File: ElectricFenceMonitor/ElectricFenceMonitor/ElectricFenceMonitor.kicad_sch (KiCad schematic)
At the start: 32 parts, among them J1 Fence wire, J2 Fence ground, J3 Power, J4 Programming, Q1 BC548, U1 Ra01_Breakout_Module, U2 PICAXE-14M2

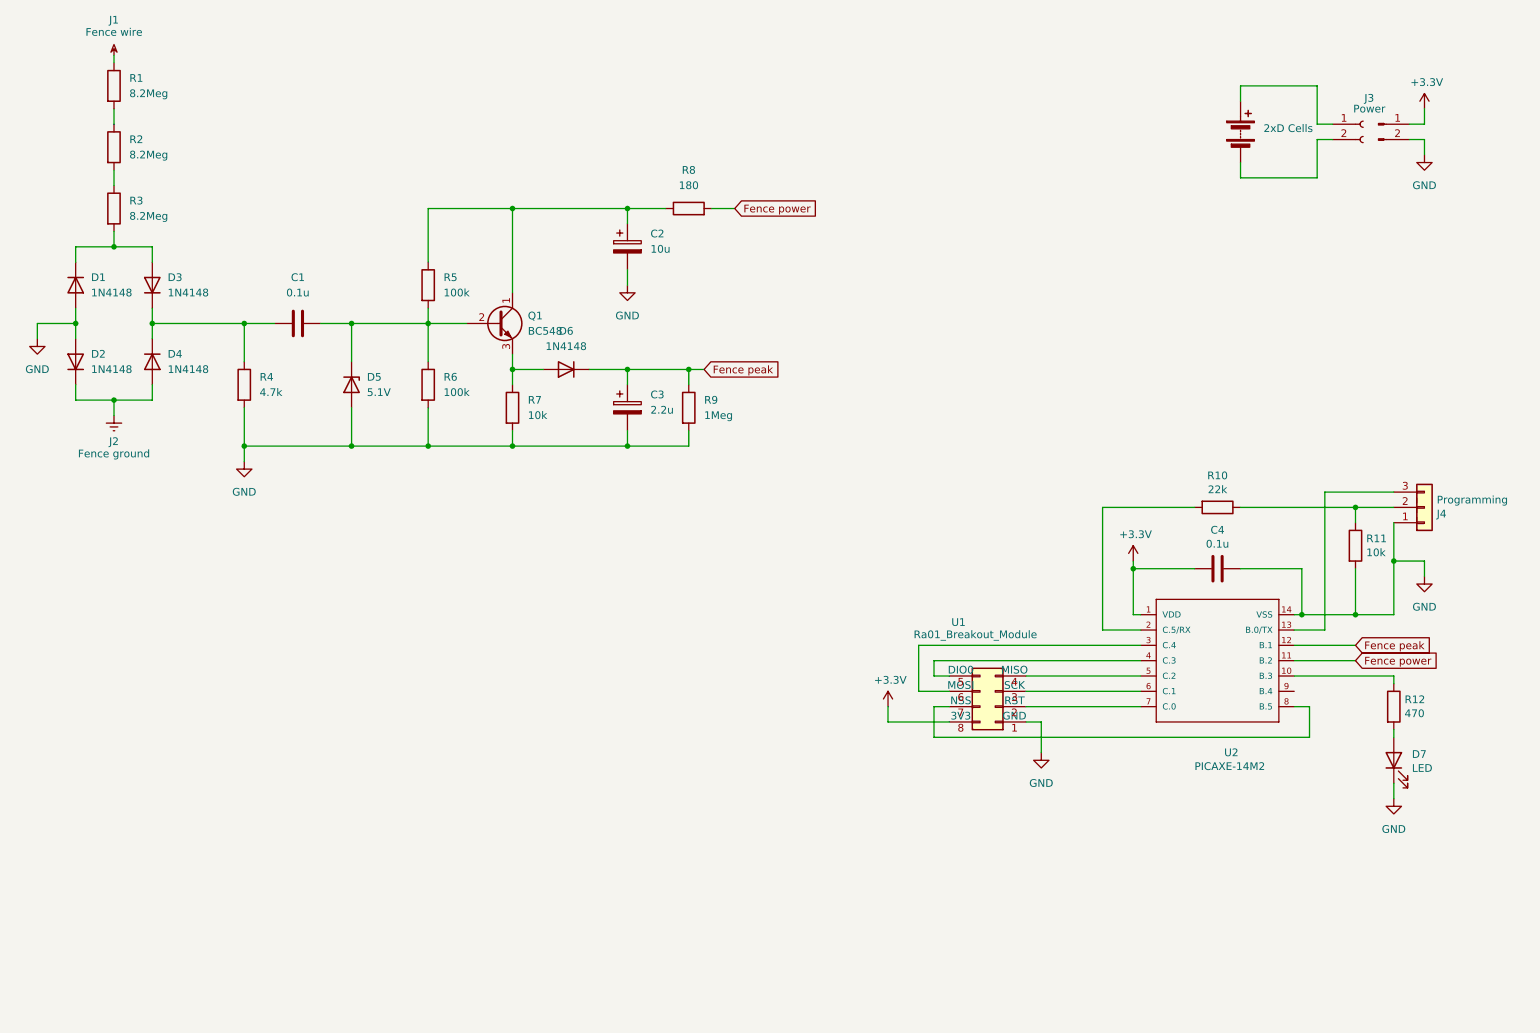
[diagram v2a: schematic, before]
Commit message: Electric fence monitor schematic updated, layout redone
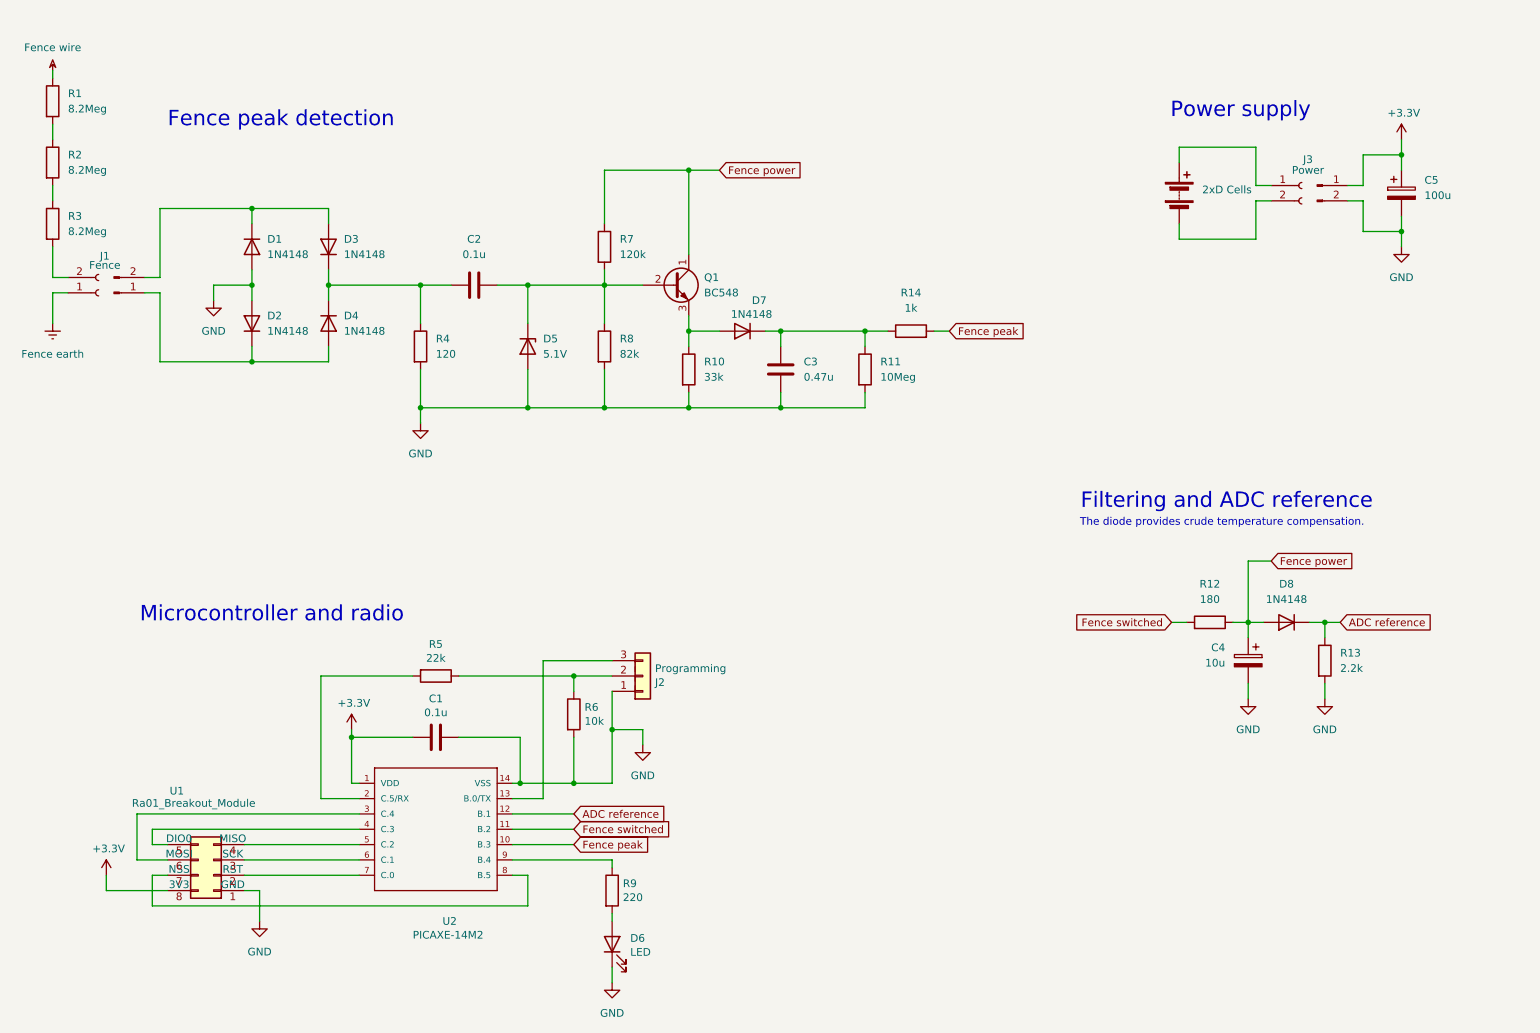
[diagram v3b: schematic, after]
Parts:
- removed C2: 10u, Capacitor_THT:CP_Radial_D6.3mm_P2.50mm, symbol Device:C_Polarized
- removed C3: 2.2u, Capacitor_THT:C_Axial_L5.1mm_D3.1mm_P10.00mm_Horizontal, symbol Device:C_Polarized
- removed J1: Fence wire, MountingHole:MountingHole_3.5mm_Pad_Via, symbol power:HT
- removed J2: Fence ground, MountingHole:MountingHole_3.5mm_Pad_Via, symbol power:GNDREF
- removed R8: 180, Resistor_THT:R_Axial_DIN0207_L6.3mm_D2.5mm_P15.24mm_Horizontal, symbol Device:R
- added #J1: Conn_01x02_Socket, symbol Connector:Conn_01x02_Socket
- added C3: 0.47u, Capacitor_THT:C_Disc_D5.0mm_W2.5mm_P5.00mm, symbol Device:C
- added C4: 10u, Capacitor_THT:CP_Radial_D13.0mm_P5.00mm, symbol Device:C_Polarized
- added C5: 100u, Capacitor_THT:CP_Radial_D13.0mm_P5.00mm, symbol Device:C_Polarized
- added D8: 1N4148, Diode_THT:D_DO-35_SOD27_P5.08mm_Vertical_KathodeUp, symbol Diode:1N4148
- added J1: Fence, TerminalBlock_Phoenix:TerminalBlock_Phoenix_MKDS-1,5-2-5.08_1x02_P5.08mm_Horizontal, symbol Connector:Conn_01x02_Pin
- added R12: 180, Resistor_THT:R_Axial_DIN0207_L6.3mm_D2.5mm_P7.62mm_Horizontal, symbol Device:R
- added R13: 2.2k, Resistor_THT:R_Axial_DIN0207_L6.3mm_D2.5mm_P7.62mm_Horizontal, symbol Device:R
- added R14: 1k, Resistor_THT:R_Axial_DIN0207_L6.3mm_D2.5mm_P7.62mm_Horizontal, symbol Device:R
- D2: footprint Diode_THT:D_DO-35_SOD27_P7.62mm_Horizontal -> Diode_THT:D_DO-35_SOD27_P5.08mm_Vertical_KathodeUp
- D4: footprint Diode_THT:D_DO-35_SOD27_P10.16mm_Horizontal -> Diode_THT:D_DO-35_SOD27_P7.62mm_Horizontal
- D5: footprint Diode_THT:D_A-405_P7.62mm_Horizontal -> Diode_THT:D_A-405_P10.16mm_Horizontal
- D7: renamed from D6; footprint Diode_THT:D_DO-35_SOD27_P5.08mm_Vertical_AnodeUp -> Diode_THT:D_DO-35_SOD27_P7.62mm_Horizontal
- R10: renamed from R7; value 10k -> 33k; footprint Resistor_THT:R_Axial_DIN0207_L6.3mm_D2.5mm_P7.62mm_Horizontal -> Resistor_THT:R_Axial_DIN0309_L9.0mm_D3.2mm_P12.70mm_Horizontal
- R11: renamed from R9; value 1Meg -> 10Meg; footprint Resistor_THT:R_Axial_DIN0207_L6.3mm_D2.5mm_P10.16mm_Horizontal -> Resistor_THT:R_Axial_DIN0207_L6.3mm_D2.5mm_P5.08mm_Vertical
- R4: value 4.7k -> 120
- R7: renamed from R5; value 100k -> 120k
- R8: renamed from R6; value 100k -> 82k; footprint Resistor_THT:R_Axial_DIN0207_L6.3mm_D2.5mm_P7.62mm_Horizontal -> Resistor_THT:R_Axial_DIN0207_L6.3mm_D2.5mm_P10.16mm_Horizontal
- R9: renamed from R12; value 470 -> 220; footprint Resistor_THT:R_Axial_DIN0309_L9.0mm_D3.2mm_P25.40mm_Horizontal -> Resistor_THT:R_Axial_DIN0207_L6.3mm_D2.5mm_P7.62mm_Horizontal
- renumbered #J1 to #J2, C4 to C1, C1 to C2, D7 to D6, J4 to J2, R10 to R5, R11 to R6
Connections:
- net +3.3V: now also C5.1
- net Fence peak: now also U2.10 (B.3), R14.2; no longer D7.1 (K), R11.1, U2.12 (B.1)
- net Fence power: now also Q1.1 (C), R7.1, C4.1, D8.2 (A), R12.1; no longer U2.11 (B.2)
- net GND: now also C3.1, C4.2, C5.2, R13.2
- net at D2.1 (K), D4.2 (A): now also J1.1 (Pin_1)
- net at D1.1 (K), D3.2 (A): now also J1.2 (Pin_2); no longer R3.2
- net Fence wire: now reaches R1.1
- net at R9.1: now also U2.9 (B.4); no longer U2.10 (B.3)
- new net: #J1.2 (Pin_2), R3.2
- new net: C3.2, D7.1 (K), R11.1, R14.1
- new net ADC reference: D8.1 (K), R13.1, U2.12 (B.1)
- new net Fence earth: #J1.1 (Pin_1)
- new net Fence switched: R12.2, U2.11 (B.2)
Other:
- note added: "Fence peak detection"
- note added: "Filtering and ADC reference"
- note added: "Microcontroller and radio"
- note added: "Power supply"
- note added: "The diode provides crude temperature compensation."
- moved on the sheet: C1, C2, D1, D2, D3, D4, D5, D6, D7, J2, J3, Q1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
